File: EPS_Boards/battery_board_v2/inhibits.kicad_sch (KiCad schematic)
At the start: 36 parts, among them J4 Conn_01x08_Male, J5 RBF, J6 Deployment Switch Bypass, U3 TPS63060, U4 LTC6995HS6-1#TRMPBF, U5 LTC6995HS6-1#TRMPBF, U6 74AUP1G08

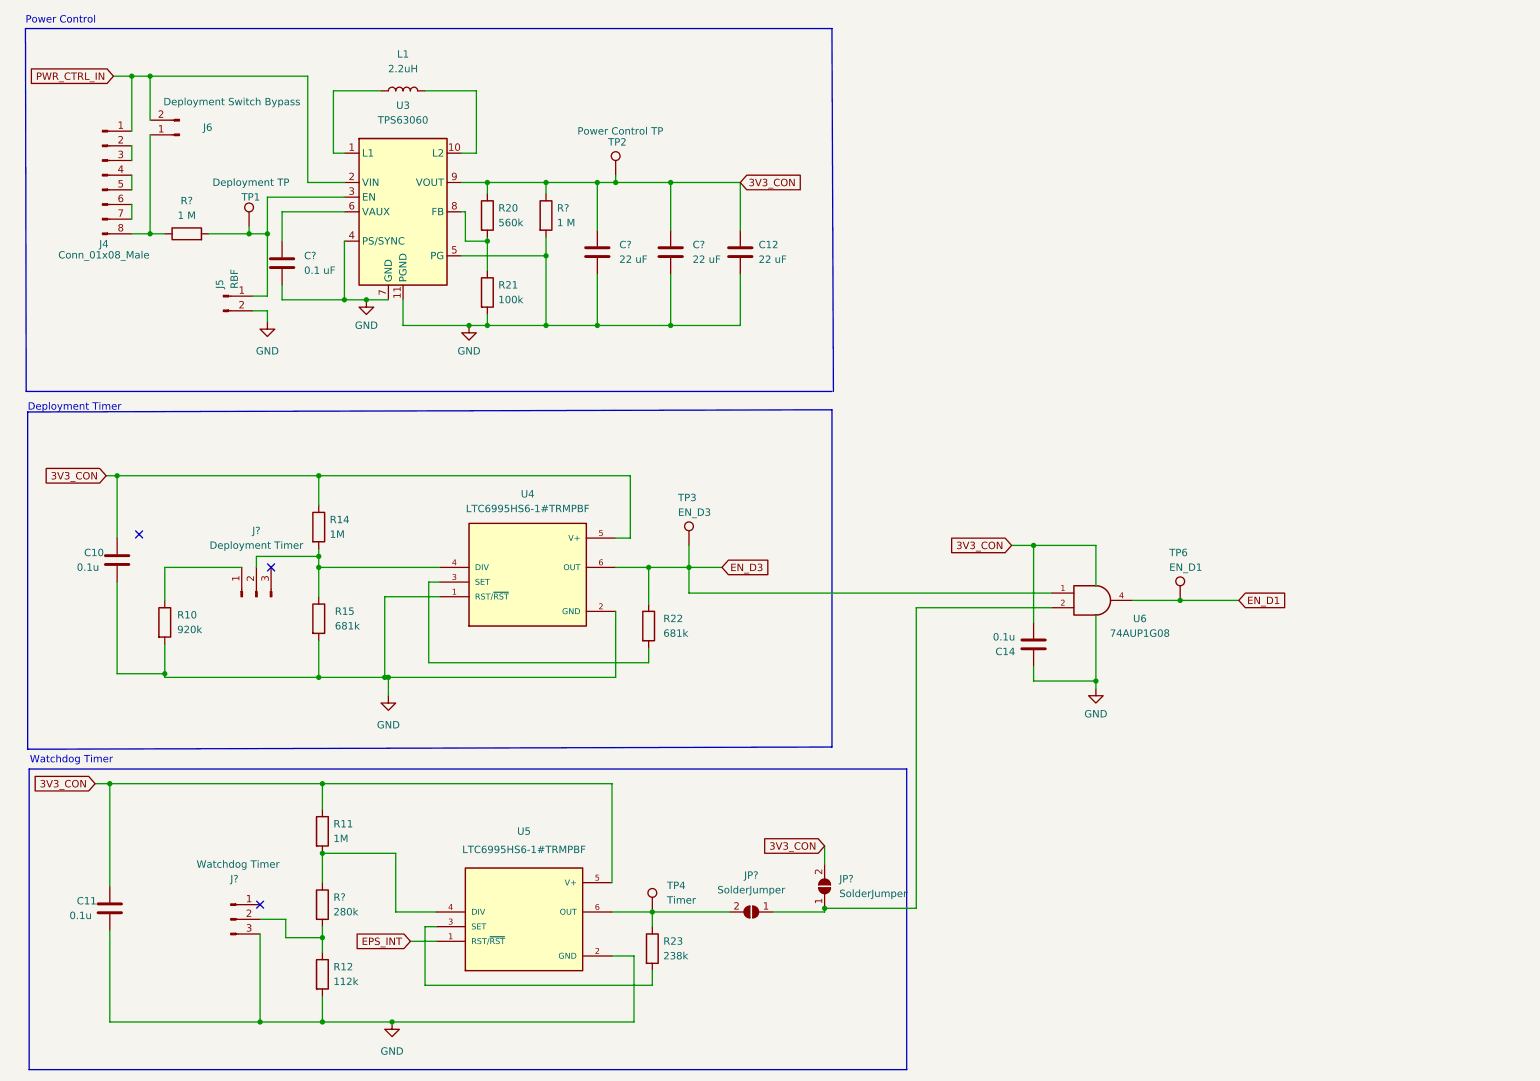
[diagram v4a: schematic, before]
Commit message: eps: battery board: design review schematic changes
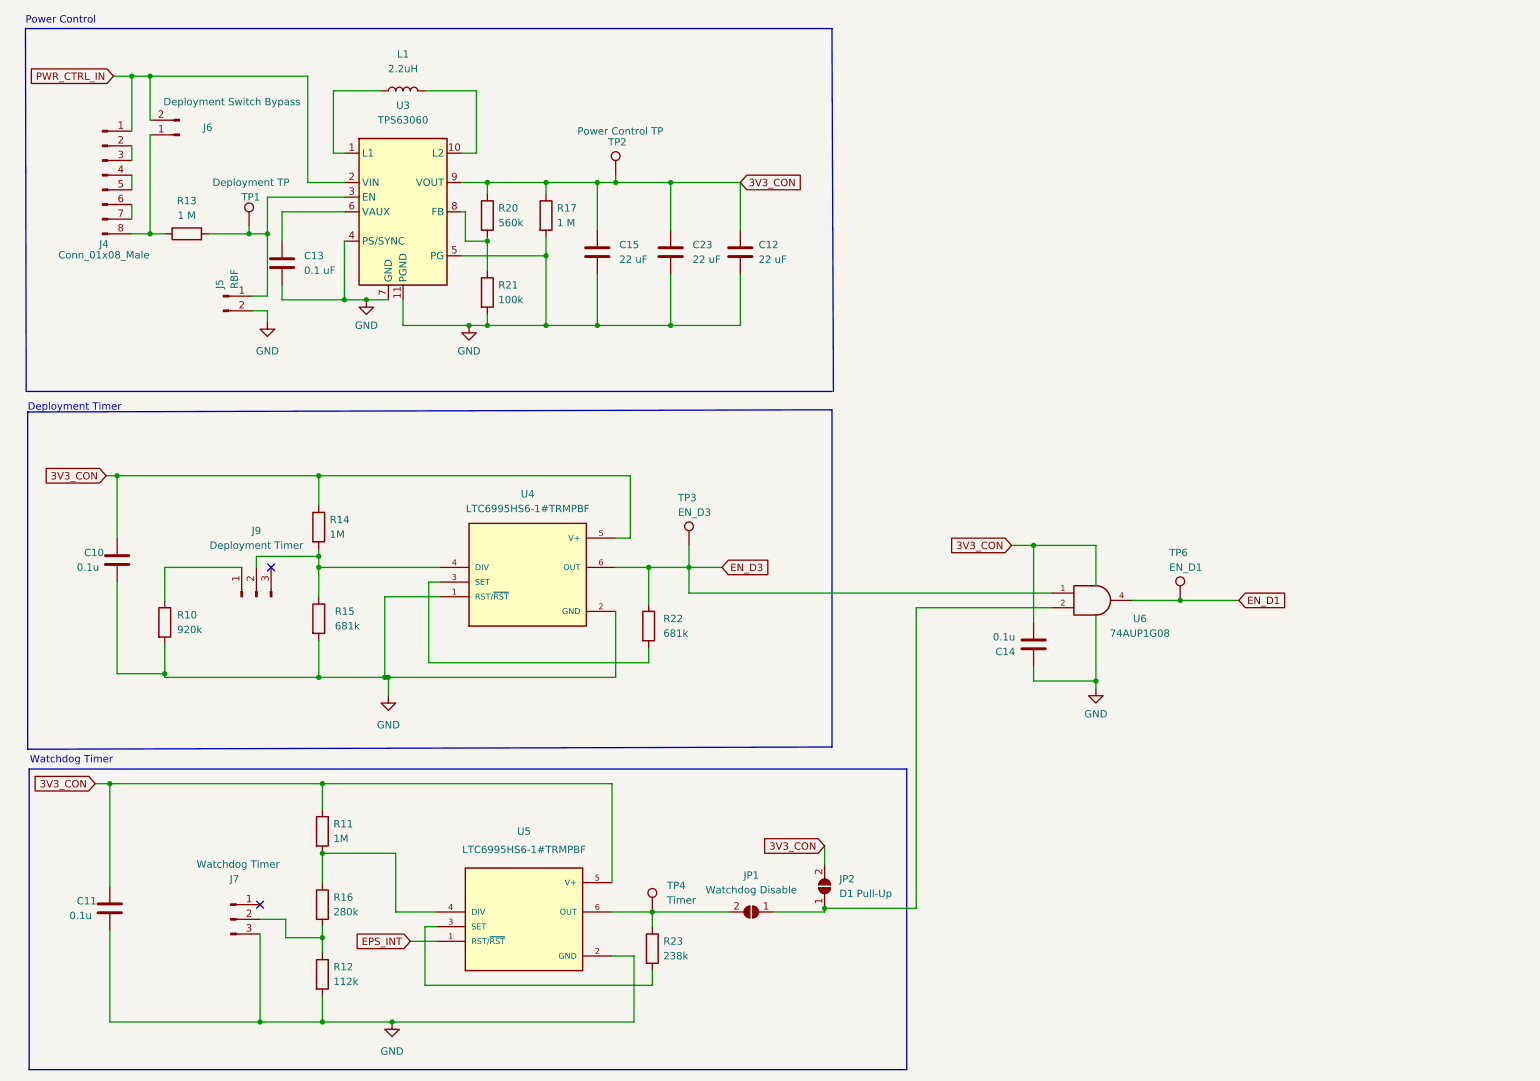
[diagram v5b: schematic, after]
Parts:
- J7, J9: renamed from J?; footprint (none) -> Connector_PinHeader_2.00mm:PinHeader_1x03_P2.00mm_Horizontal
- JP1: renamed from JP?; value SolderJumper -> Watchdog Disable
- JP2: renamed from JP?; value SolderJumper -> D1 Pull-Up
- R13, R17: renamed from R?; footprint (none) -> Resistor_SMD:R_0402_1005Metric
- gave numbers to parts that had none: 4
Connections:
- no-connect marks 3 -> 2
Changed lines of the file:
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@@
   )
   (no_connect (at 57.785 109.22))
-  (no_connect (at 34.925 103.505))
   (no_connect (at 55.88 167.64))
   (wire (pts (xy 29.21 93.345) (xy 31.115 93.345))
@@
   (symbol (lib_id "Device:R") (at 43.18 51.435 90) (unit 1)
     (in_bom yes) (on_board yes) (fields_autoplaced)
-    (property "Reference" "R?" (id 0) (at 43.18 45.72 90))
+    (property "Reference" "R13" (id 0) (at 43.18 45.72 90))
     (property "Value" "1 M" (id 1) (at 43.18 48.26 90))
-    (property "Footprint" "" (id 2) (at 43.18 53.213 90)
+    (property "Footprint" "Resistor_SMD:R_0402_1005Metric" (id 2) (at 43.18 53.213 90)
       (effects (font (size 1.27 1.27)) hide)
     )
@@
   (symbol (lib_id "Jumper:SolderJumper_2_Open") (at 140.97 168.91 180) (unit 1)
     (in_bom yes) (on_board yes) (fields_autoplaced)
-    (property "Reference" "JP?" (id 0) (at 140.97 162.56 0))
-    (property "Value" "SolderJumper" (id 1) (at 140.97 165.1 0))
+    (property "Reference" "JP1" (id 0) (at 140.97 162.56 0))
+    (property "Value" "Watchdog Disable" (id 1) (at 140.97 165.1 0))
     (property "Footprint" "Jumper:SolderJumper-2_P1.3mm_Open_Pad1.0x1.5mm" (id 2) (at 140.97 168.91 0)
       (effects (font (size 1.27 1.27)) hide)
@@
   (symbol (lib_id "Connector:Conn_01x03_Male") (at 55.245 114.3 90) (unit 1)
     (in_bom yes) (on_board yes)
-    (property "Reference" "J?" (id 0) (at 55.245 102.87 90))
+    (property "Reference" "J9" (id 0) (at 55.245 102.87 90))
     (property "Value" "Deployment Timer" (id 1) (at 55.245 105.41 90))
-    (property "Footprint" "" (id 2) (at 55.245 114.3 0)
+    (property "Footprint" "Connector_PinHeader_2.00mm:PinHeader_1x03_P2.00mm_Horizontal" (id 2) (at 55.245 114.3 0)
       (effects (font (size 1.27 1.27)) hide)
     )
@@
   (symbol (lib_id "Device:C") (at 59.69 56.515 0) (unit 1)
     (in_bom yes) (on_board yes)
-    (property "Reference" "C?" (id 0) (at 63.5 55.2449 0)
+    (property "Reference" "C13" (id 0) (at 63.5 55.2449 0)
       (effects (font (size 1.27 1.27)) (justify left))
     )
@@
   (symbol (lib_id "Connector:Conn_01x03_Male") (at 50.8 170.18 0) (unit 1)
     (in_bom yes) (on_board yes)
-    (property "Reference" "J?" (id 0) (at 51.435 163.195 0))
+    (property "Reference" "J7" (id 0) (at 51.435 163.195 0))
     (property "Value" "Watchdog Timer" (id 1) (at 52.07 160.655 0))
-    (property "Footprint" "" (id 2) (at 50.8 170.18 0)
+    (property "Footprint" "Connector_PinHeader_2.00mm:PinHeader_1x03_P2.00mm_Horizontal" (id 2) (at 50.8 170.18 0)
       (effects (font (size 1.27 1.27)) hide)
     )
@@
   (symbol (lib_id "Device:C") (at 114.3 54.61 0) (unit 1)
     (in_bom yes) (on_board yes) (fields_autoplaced)
-    (property "Reference" "C?" (id 0) (at 118.11 53.3399 0)
+    (property "Reference" "C15" (id 0) (at 118.11 53.3399 0)
       (effects (font (size 1.27 1.27)) (justify left))
     )
@@
   (symbol (lib_id "Device:R") (at 66.675 167.64 0) (unit 1)
     (in_bom yes) (on_board yes) (fields_autoplaced)
-    (property "Reference" "R?" (id 0) (at 68.58 166.3699 0)
+    (property "Reference" "R16" (id 0) (at 68.58 166.3699 0)
       (effects (font (size 1.27 1.27)) (justify left))
     )
@@
   (symbol (lib_id "Device:R") (at 105.41 48.26 0) (unit 1)
     (in_bom yes) (on_board yes) (fields_autoplaced)
-    (property "Reference" "R?" (id 0) (at 107.315 46.9899 0)
+    (property "Reference" "R17" (id 0) (at 107.315 46.9899 0)
       (effects (font (size 1.27 1.27)) (justify left))
     )
@@
       (effects (font (size 1.27 1.27)) (justify left))
     )
-    (property "Footprint" "" (id 2) (at 103.632 48.26 90)
+    (property "Footprint" "Resistor_SMD:R_0402_1005Metric" (id 2) (at 103.632 48.26 90)
       (effects (font (size 1.27 1.27)) hide)
     )
@@
   (symbol (lib_id "power:GND") (at 74.295 62.865 0) (unit 1)
     (in_bom yes) (on_board yes) (fields_autoplaced)
-    (property "Reference" "#PWR?" (id 0) (at 74.295 69.215 0)
+    (property "Reference" "#PWR01" (id 0) (at 74.295 69.215 0)
       (effects (font (size 1.27 1.27)) hide)
     )
@@
   (symbol (lib_id "Jumper:SolderJumper_2_Open") (at 153.67 164.465 90) (unit 1)
     (in_bom yes) (on_board yes) (fields_autoplaced)
-    (property "Reference" "JP?" (id 0) (at 156.21 163.1949 90)
+    (property "Reference" "JP2" (id 0) (at 156.21 163.1949 90)
       (effects (font (size 1.27 1.27)) (justify right))
     )
-    (property "Value" "SolderJumper" (id 1) (at 156.21 165.7349 90)
+    (property "Value" "D1 Pull-Up" (id 1) (at 156.21 165.7349 90)
       (effects (font (size 1.27 1.27)) (justify right))
     )
@@
   (symbol (lib_id "Device:C") (at 127 54.61 0) (unit 1)
     (in_bom yes) (on_board yes) (fields_autoplaced)
-    (property "Reference" "C?" (id 0) (at 130.81 53.3399 0)
-      (effects (font (size 1.27 1.27)) (justify left))
-    )
+    (property "Reference" "C23" (id 0) (at 130.81 53.3399 0)
+      (effects (font (size 1.27 1.27)) (justify left))
+    )

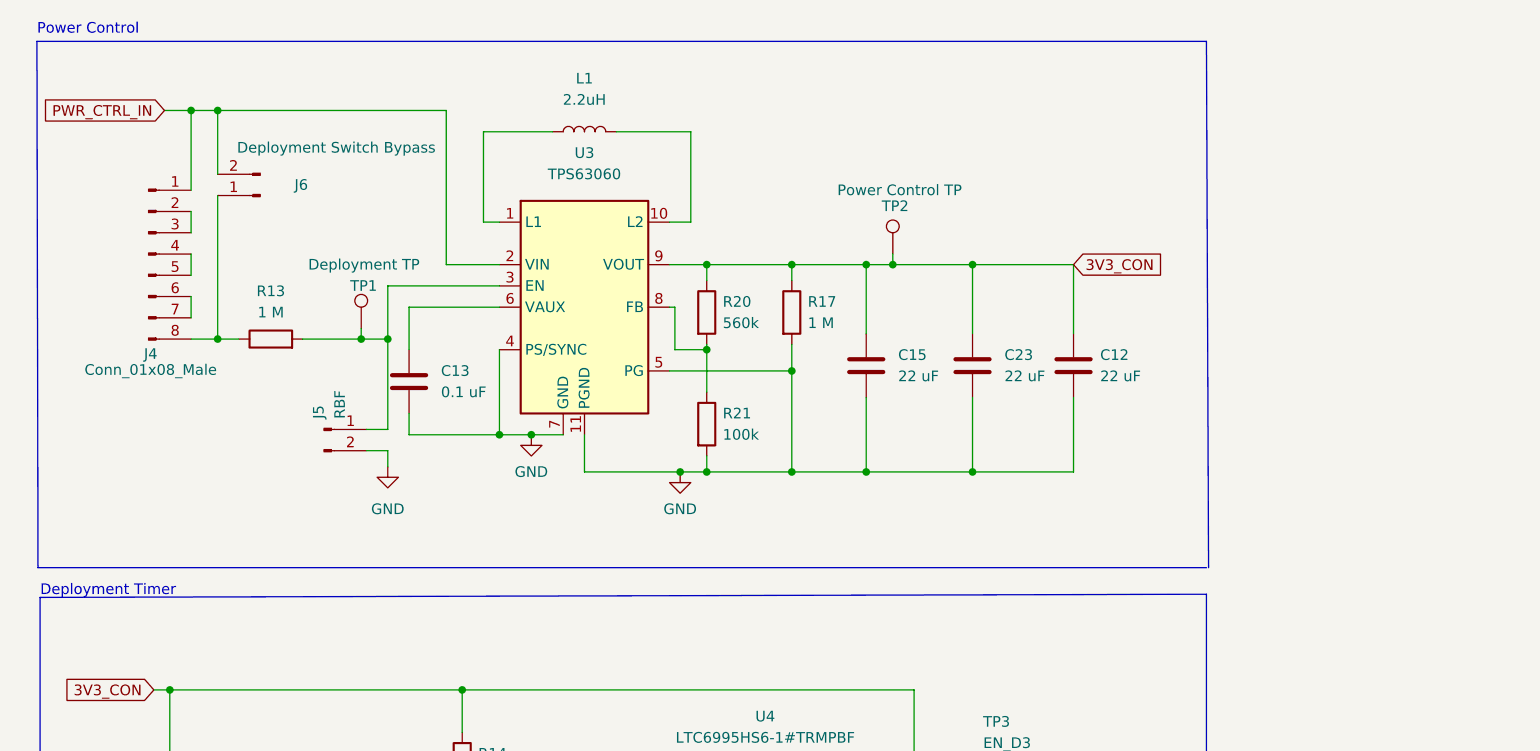
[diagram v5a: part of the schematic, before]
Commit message: eps: battery board: post-layout review changes
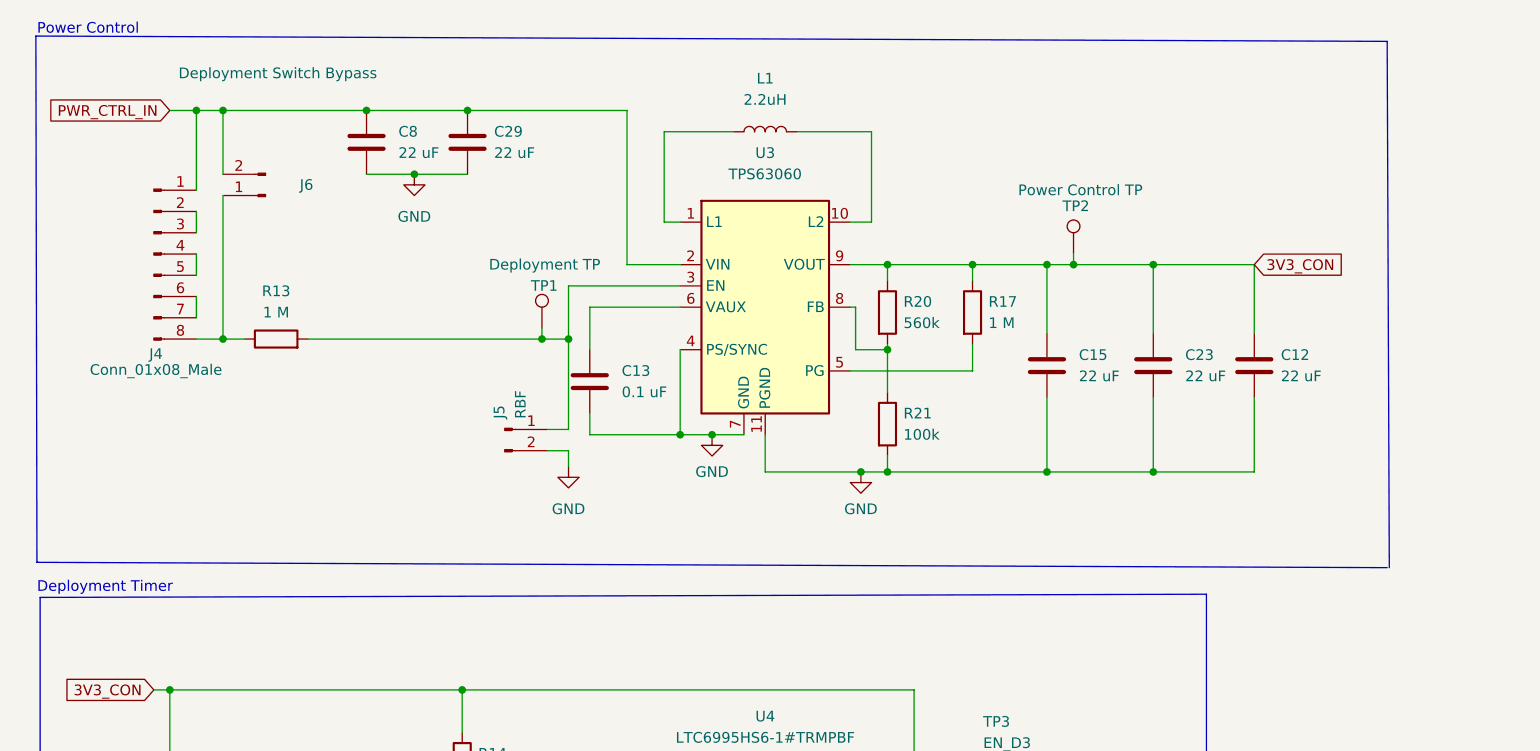
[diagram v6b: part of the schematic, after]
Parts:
- added C29, C8: 22 uF, Capacitor_SMD:C_01005_0402Metric, symbol Device:C
- TP1, TP2, TP3, TP4, TP6: footprint TestPoint:TestPoint_Pad_D2.0mm -> TestPoint:TestPoint_THTPad_D2.0mm_Drill1.0mm
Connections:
- net GND: now also C29.2, C8.2; no longer R17.2, U3.5 (PG)
- net PWR_CTRL_IN: now also C29.1, C8.1
- new net: R17.2, U3.5 (PG)
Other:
- moved on the sheet: C12, C13, C15, C23, J4, J5, J6, L1, R13, R17, R20, R21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

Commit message: eps: battery board: update footprints on basic components to 0603
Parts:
- C10: footprint Capacitor_SMD:C_01005_0402Metric -> Capacitor_SMD:C_0603_1608Metric
- C12, C13, C15, C23, C29, C8: footprint Capacitor_SMD:C_01005_0402Metric -> Capacitor_SMD:C_0402_1005Metric
- C14: footprint Capacitor_SMD:C_0402_1005Metric -> Capacitor_SMD:C_0603_1608Metric
- R13: footprint Resistor_SMD:R_0402_1005Metric -> Resistor_SMD:R_0603_1608Metric
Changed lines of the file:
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@@
     (property "Reference" "R13" (id 0) (at 43.815 45.72 90))
     (property "Value" "1 M" (id 1) (at 43.815 48.26 90))
-    (property "Footprint" "Resistor_SMD:R_0402_1005Metric" (id 2) (at 43.815 53.213 90)
+    (property "Footprint" "Resistor_SMD:R_0603_1608Metric" (id 2) (at 43.815 53.213 90)
       (effects (font (size 1.27 1.27)) hide)
     )
@@
       (effects (font (size 1.27 1.27)) (justify left))
     )
-    (property "Footprint" "Capacitor_SMD:C_01005_0402Metric" (id 2) (at 55.5752 31.75 0)
+    (property "Footprint" "Capacitor_SMD:C_0402_1005Metric" (id 2) (at 55.5752 31.75 0)
       (effects (font (size 1.27 1.27)) hide)
     )
@@
       (effects (font (size 1.27 1.27)) (justify left))
     )
-    (property "Footprint" "Capacitor_SMD:C_01005_0402Metric" (id 2) (at 32.0802 111.76 0)
+    (property "Footprint" "Capacitor_SMD:C_0603_1608Metric" (id 2) (at 32.0802 111.76 0)
       (effects (font (size 1.27 1.27)) hide)
     )
@@
       (effects (font (size 1.27 1.27)) (justify left))
     )
-    (property "Footprint" "Capacitor_SMD:C_01005_0402Metric" (id 2) (at 82.2452 60.325 0)
+    (property "Footprint" "Capacitor_SMD:C_0402_1005Metric" (id 2) (at 82.2452 60.325 0)
       (effects (font (size 1.27 1.27)) hide)
     )
@@
       (effects (font (size 1.27 1.27)) (justify left))
     )
-    (property "Footprint" "Capacitor_SMD:C_0402_1005Metric" (id 2) (at 188.8998 118.745 0)
+    (property "Footprint" "Capacitor_SMD:C_0603_1608Metric" (id 2) (at 188.8998 118.745 0)
       (effects (font (size 1.27 1.27)) hide)
     )
@@
       (effects (font (size 1.27 1.27)) (justify left))
     )
-    (property "Footprint" "Capacitor_SMD:C_01005_0402Metric" (id 2) (at 136.8552 58.42 0)
+    (property "Footprint" "Capacitor_SMD:C_0402_1005Metric" (id 2) (at 136.8552 58.42 0)
       (effects (font (size 1.27 1.27)) hide)
     )
@@
       (effects (font (size 1.27 1.27)) (justify left))
     )
-    (property "Footprint" "Capacitor_SMD:C_01005_0402Metric" (id 2) (at 67.6402 31.75 0)
+    (property "Footprint" "Capacitor_SMD:C_0402_1005Metric" (id 2) (at 67.6402 31.75 0)
       (effects (font (size 1.27 1.27)) hide)
     )
@@
       (effects (font (size 1.27 1.27)) (justify left))
     )
-    (property "Footprint" "Capacitor_SMD:C_01005_0402Metric" (id 2) (at 161.6202 58.42 0)
+    (property "Footprint" "Capacitor_SMD:C_0402_1005Metric" (id 2) (at 161.6202 58.42 0)
       (effects (font (size 1.27 1.27)) hide)
     )
@@
       (effects (font (size 1.27 1.27)) (justify left))
     )
-    (property "Footprint" "Capacitor_SMD:C_01005_0402Metric" (id 2) (at 149.5552 58.42 0)
-      (effects (font (size 1.27 1.27)) hide)
-    )
+    (property "Footprint" "Capacitor_SMD:C_0402_1005Metric" (id 2) (at 149.5552 58.42 0)
+      (effects (font (size 1.27 1.27)) hide)
+    )

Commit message: eps: battery board: include updated manufacuring files
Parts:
- C10: footprint Capacitor_SMD:C_0603_1608Metric -> Capacitor_SMD:C_0402_1005Metric
- U4, U5: footprint qset-footprints:SOT95P280X100-6N -> qset-footprints:DFN-6_DCB_LIT
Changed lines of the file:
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@@
       (effects (font (size 1.27 1.27)) (justify left))
     )
-    (property "Footprint" "Capacitor_SMD:C_0603_1608Metric" (id 2) (at 32.0802 111.76 0)
+    (property "Footprint" "Capacitor_SMD:C_0402_1005Metric" (id 2) (at 32.0802 111.76 0)
       (effects (font (size 1.27 1.27)) hide)
     )
@@
     (property "Reference" "U5" (id 0) (at 101.6 154.94 0))
     (property "Value" "LTC6995HS6-1#TRMPBF" (id 1) (at 101.6 158.115 0))
-    (property "Footprint" "qset-footprints:SOT95P280X100-6N" (id 2) (at 101.6 168.91 0)
+    (property "Footprint" "qset-footprints:DFN-6_DCB_LIT" (id 2) (at 101.6 168.91 0)
       (effects (font (size 1.27 1.27)) (justify bottom) hide)
     )
@@
     (property "Reference" "U4" (id 0) (at 102.235 96.52 0))
     (property "Value" "LTC6995HS6-1#TRMPBF" (id 1) (at 102.235 99.06 0))
-    (property "Footprint" "qset-footprints:SOT95P280X100-6N" (id 2) (at 102.235 109.22 0)
-      (effects (font (size 1.27 1.27)) (justify bottom) hide)
-    )
+    (property "Footprint" "qset-footprints:DFN-6_DCB_LIT" (id 2) (at 102.235 109.22 0)
+      (effects (font (size 1.27 1.27)) (justify bottom) hide)
+    )
